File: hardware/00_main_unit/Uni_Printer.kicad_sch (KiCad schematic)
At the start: 9 parts, among them J5 FIDUCIAL, J6 FIDUCIAL

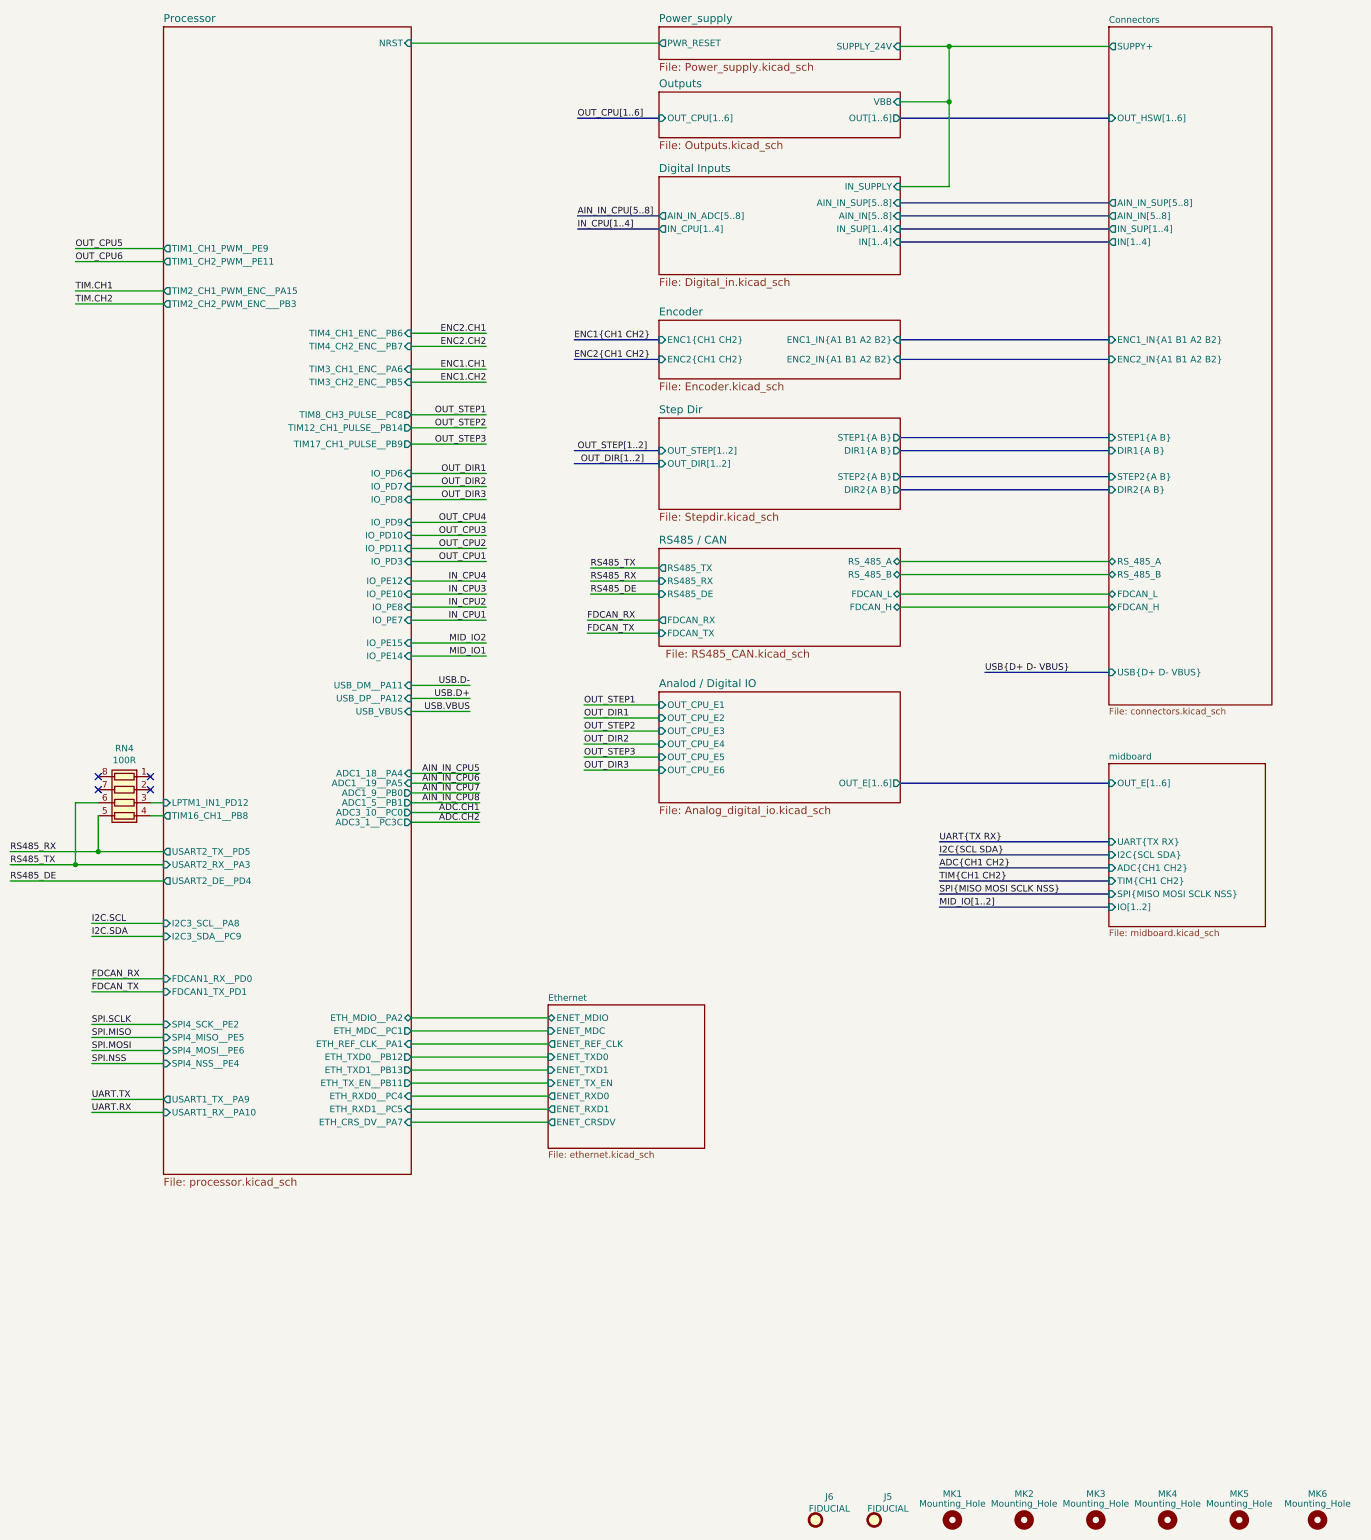
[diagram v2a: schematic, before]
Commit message: Remote mode fixes
Signed-off-by: Jarosław Karwik <jaroslaw.karwik@gmail.com>
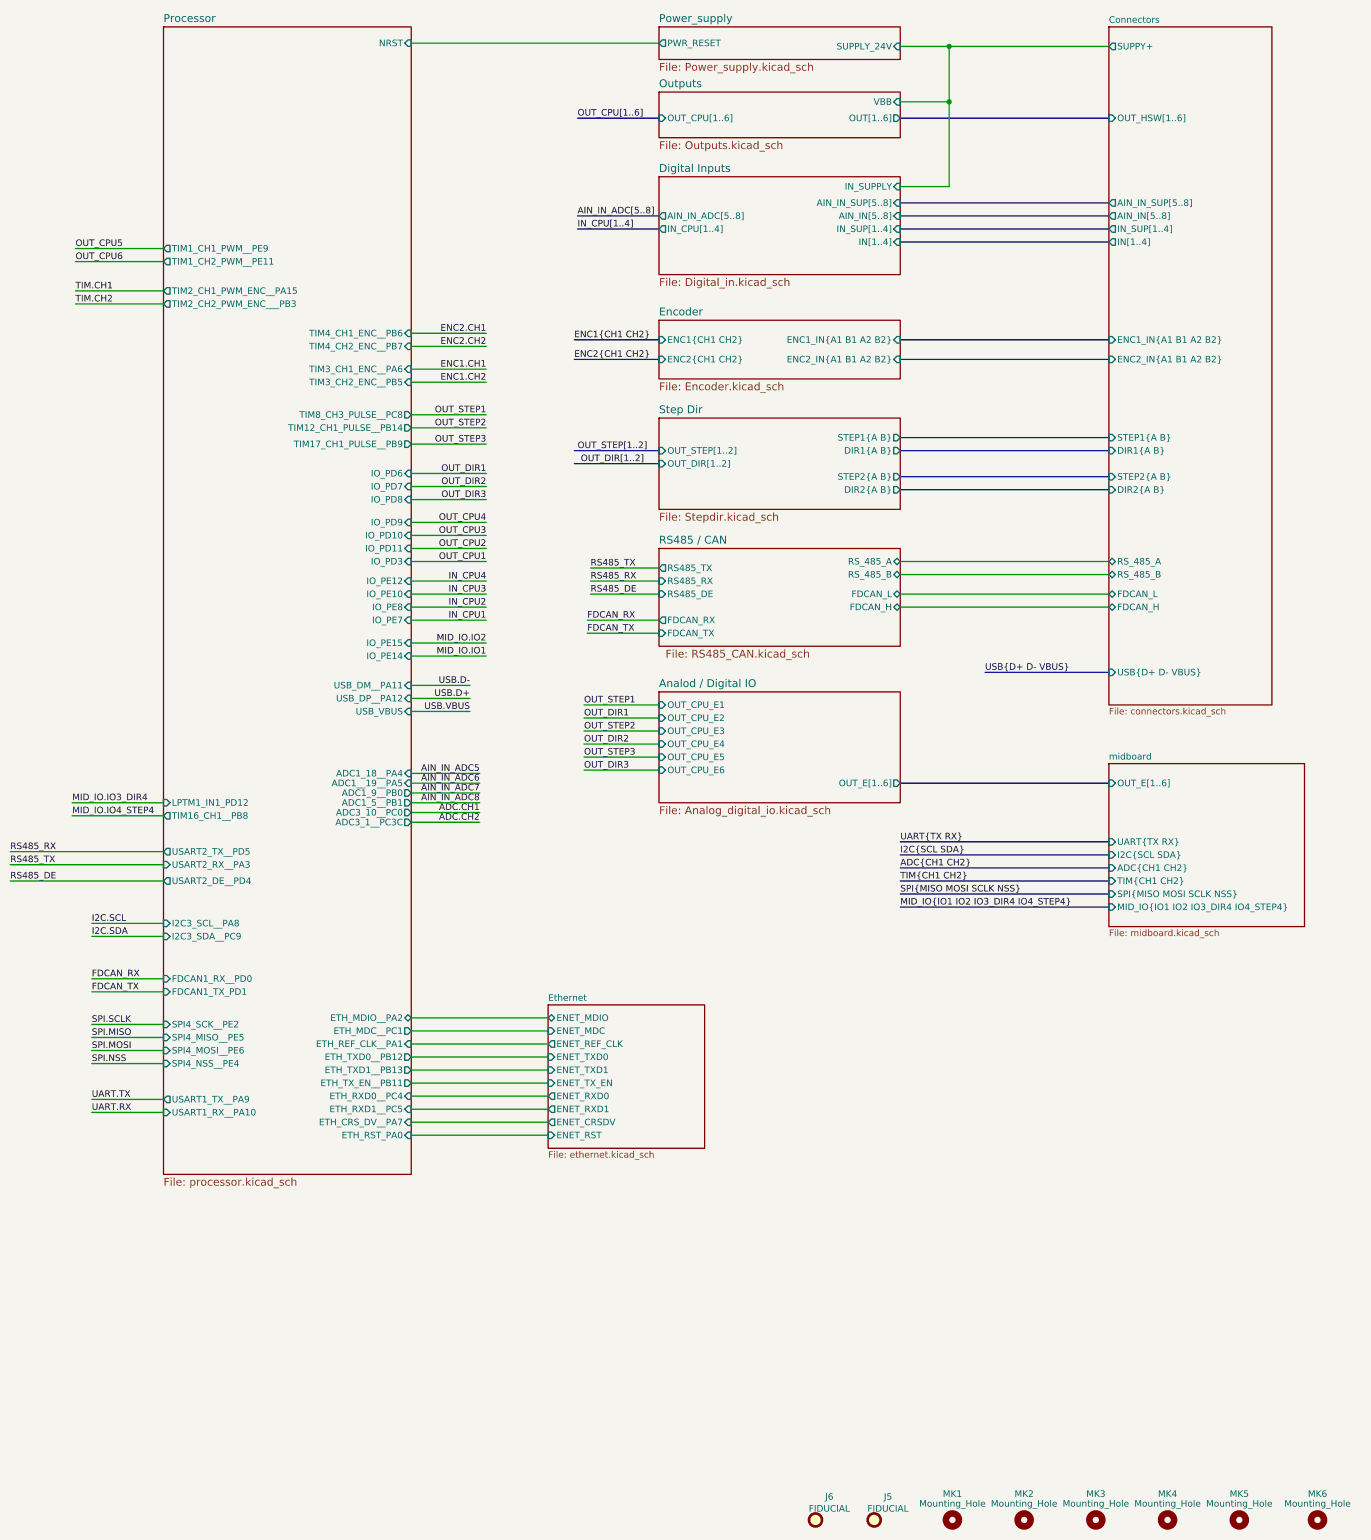
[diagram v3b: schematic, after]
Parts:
- removed RN4: 100R, moje:R_Array_Convex_4x0603, symbol Uni_Printer-rescue:R_Pack04-Device
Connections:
- no-connect marks 4 -> 0
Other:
- sheet Ethernet ports: added ENET_RST; removed none
- sheet Processor ports: added ETH_RST_PA0; removed none
- sheet midboard ports: added MID_IO{IO1 IO2 IO3_DIR4 IO4_STEP4}; removed IO[1..2]

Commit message: FW and SW updates for new revision
Signed-off-by: Jarosław Karwik <jaroslaw.karwik@gmail.com>
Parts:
- J5, J6: now left out of the parts list
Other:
- sheet Analod / Digital IO renamed Analog  Digital IO
- removed sheet RS485 / CAN
- removed sheet midboard
- sheet Analog  Digital IO ports: added ADC{CH1 CH2}, I2C_DIFF{SCL_TX SCL_RX  SDA_TX SDA_RX}, I2C{SCL SDA}, OUT_CPU_DIR1, OUT_CPU_DIR2, OUT_CPU_DIR3, OUT_CPU_DIR8, OUT_CPU_STEP1, OUT_CPU_STEP2, OUT_CPU_STEP3, OUT_CPU_STEP8; removed OUT_CPU_E1, OUT_CPU_E2, OUT_CPU_E3, OUT_CPU_E4, OUT_CPU_E5, OUT_CPU_E6, OUT_E[1..6]
- sheet Connectors ports: added DIFF_IN{A1 B1 A2 B2}, DIR3{A B}, DIR4{A B}, DIR5{A B}, DIR6{A B}, DIR7{A B}, ENC3_IN{A1 B1 A2 B2}, I2C_DIFF{SCL_TX SCL_RX  SDA_TX SDA_RX}, STEP3{A B}, STEP4{A B}, STEP5{A B}, STEP6{A B}, STEP7{A B}; removed FDCAN_H, FDCAN_L, RS_485_A, RS_485_B
- sheet Encoder ports: added DIFF_IN{A1 B1 A2 B2}, ENC3_IN{A1 B1 A2 B2}, ENC3{CH1 CH2}, IN10_CPU, IN9_CPU; removed none
- sheet Processor ports: added IO_PA10, IO_PA9, IO_PB8, IO_PD1, IO_PD12, IO_PD2; removed FDCAN1_RX__PD0, FDCAN1_TX_PD1, LPTM1_IN1_PD12, TIM16_CH1__PB8, USART1_RX__PA10, USART1_TX__PA9, USART2_DE__PD4, USART2_RX__PA3, USART2_TX__PD5
- sheet Step Dir ports: added DIR3{A B}, DIR4{A B}, DIR5{A B}, DIR6{A B}, DIR7{A B}, OUT_DIR[1..7], OUT_STEP[1..7], STEP3{A B}, STEP4{A B}, STEP5{A B}, STEP6{A B}, STEP7{A B}; removed OUT_DIR[1..2], OUT_STEP[1..2]
